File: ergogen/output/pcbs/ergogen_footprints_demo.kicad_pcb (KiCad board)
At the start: 2 copper layers, 95 x 95 mm, 51 parts

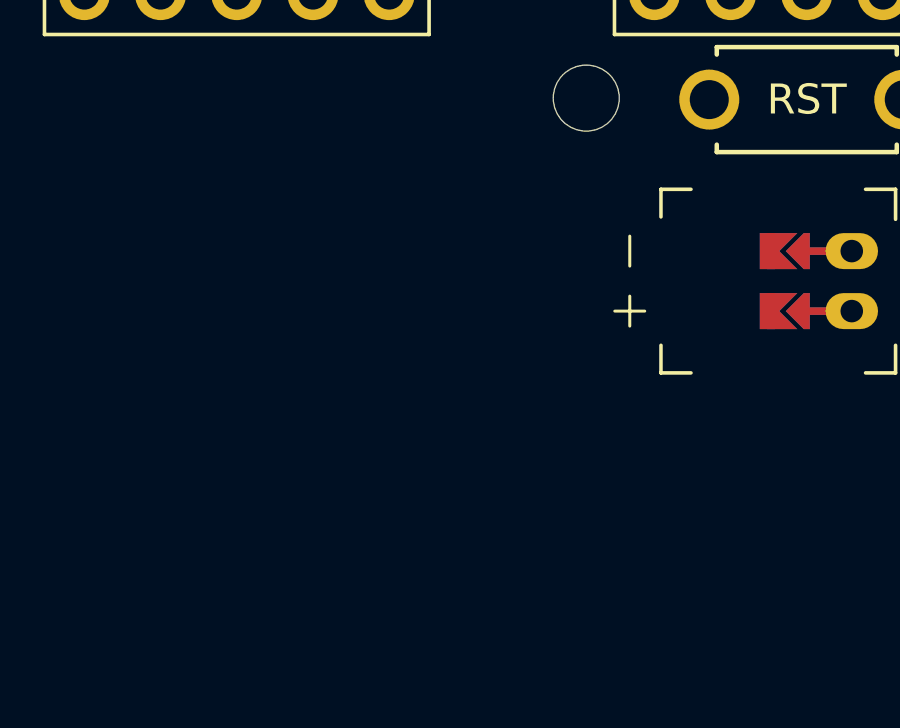
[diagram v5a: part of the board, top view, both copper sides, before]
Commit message: Add alternate power switch behavior
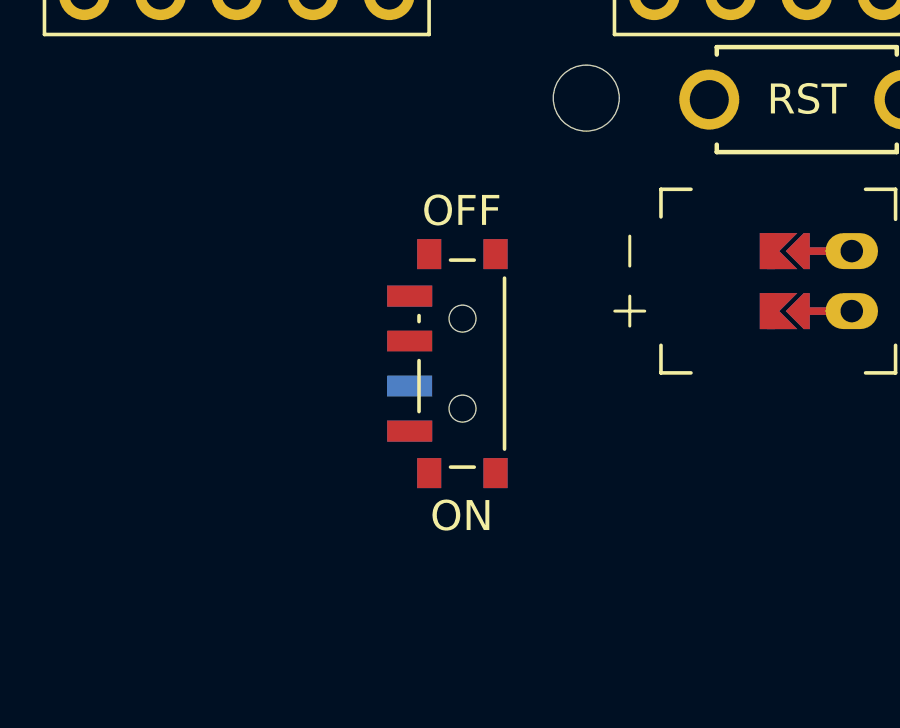
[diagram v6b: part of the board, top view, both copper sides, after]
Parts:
- added PWR2: reset_button, ceoloide:power_switch_smd_side, F.Cu at (107.5, 101.5)
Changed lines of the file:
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@@
     (segment (start 102.540 89.200) (end 102.540 87.450) (width 0.25) (layer "B.Cu") (net 63))
     (segment (start 105.080 89.200) (end 105.080 87.450) (width 0.25) (layer "B.Cu") (net 62))
+      (module "ceoloide:power_switch_smd_side" (layer F.Cu)
+        (at 107.5 101.5 0)
+        (attr smd)
+        (fp_text value "reset_button" (at 0 2.5 0) (layer F.Fab)
+          (effects (font (size 1 1) (thickness 0.15)))
+        )
+        (fp_line (start -1.305 -3.35) (end -1.305 3.35) (layer F.Fab) (width 0.1))
+        (fp_line (start 1.295 -3.35) (end -1.305 -3.35) (layer F.Fab) (width 0.1))
+        (fp_line (start 1.295 3.35) (end 1.295 -3.35) (layer F.Fab) (width 0.1))
+        (fp_line (start -1.305 3.35) (end 1.295 3.35) (layer F.Fab) (width 0.1))
+        (fp_line (start 2.595 0.1) (end 1.295 0.1) (layer F.Fab) (width 0.1))
+        (fp_line (start 2.645 0.15) (end 2.595 0.1) (layer F.Fab) (width 0.1))
+        (fp_line (start 2.845 0.35) (end 2.645 0.15) (layer F.Fab) (width 0.1))
+        (fp_line (start 2.845 1.2) (end 2.845 0.35) (layer F.Fab) (width 0.1))
+        (fp_line (start 2.645 1.4) (end 2.845 1.2) (layer F.Fab) (width 0.1))
+        (fp_line (start 1.345 1.4) (end 2.645 1.4) (layer F.Fab) (width 0.1))
+        (pad "" smd rect (at 1.125 -3.65 90) (size 1 0.8) (layers F.Cu F.Paste F.Mask))
+        (pad "" smd rect (at -1.085 -3.65 90) (size 1 0.8) (layers F.Cu F.Paste F.Mask))
+        (pad "" smd rect (at -1.085 3.65 90) (size 1 0.8) (layers F.Cu F.Paste F.Mask))
+        (pad "" smd rect (at 1.125 3.65 90) (size 1 0.8) (layers F.Cu F.Paste F.Mask))
+        (pad 1 smd rect (at -1.735 2.25 90) (size 0.7 1.5) (layers F.Cu F.Paste F.Mask) (net 97 "BAT_P"))
+        (pad 2 smd rect (at -1.735 -0.75 90) (size 0.7 1.5) (layers F.Cu F.Paste F.Mask) (net 18 "RAW"))
+        (pad 3 smd rect (at -1.735 -2.25 90) (size 0.7 1.5) (layers F.Cu F.Paste F.Mask) )
+        (fp_text reference "PWR2" (at -3.6 0 -90) (layer F.SilkS) hide
+          (effects (font (size 1 1) (thickness 0.15)))
+        )
+        (fp_text user "ON" (at 0 4.5 0) (layer "F.SilkS")
+          (effects (font (size 1 1) (thickness 0.15)) (justify top))
+        )
+        (fp_text user "OFF" (at 0 -4.5 0) (layer "F.SilkS")
+          (effects (font (size 1 1) (thickness 0.15)) (justify bottom))
+        )
+        (fp_line (start 0.415 -3.45) (end -0.375 -3.45) (layer F.SilkS) (width 0.12))
+        (fp_line (start -0.375 3.45) (end 0.415 3.45) (layer F.SilkS) (width 0.12))
+        (fp_line (start -1.425 1.6) (end -1.425 -0.1) (layer F.SilkS) (width 0.12))
+        (fp_line (start 1.425 2.85) (end 1.425 -2.85) (layer F.SilkS) (width 0.12))
+        (fp_line (start -1.425 -1.4) (end -1.425 -1.6) (layer F.SilkS) (width 0.12))
+        (fp_line (start 2.595 -0.1) (end 1.295 -0.1) (layer B.Fab) (width 0.1))
+        (fp_line (start -1.305 3.35) (end -1.305 -3.35) (layer B.Fab) (width 0.1))
+        (fp_line (start 2.645 -0.15) (end 2.595 -0.1) (layer B.Fab) (width 0.1))
+        (fp_line (start 2.845 -1.2) (end 2.845 -0.35) (layer B.Fab) (width 0.1))
+        (fp_line (start 1.345 -1.4) (end 2.645 -1.4) (layer B.Fab) (width 0.1))
+        (fp_line (start 2.845 -0.35) (end 2.645 -0.15) (layer B.Fab) (width 0.1))
+        (fp_line (start 2.645 -1.4) (end 2.845 -1.2) (layer B.Fab) (width 0.1))
+        (fp_line (start 1.295 -3.35) (end 1.295 3.35) (layer B.Fab) (width 0.1))
+        (fp_line (start 1.295 3.35) (end -1.305 3.35) (layer B.Fab) (width 0.1))
+        (fp_line (start -1.305 -3.35) (end 1.295 -3.35) (layer B.Fab) (width 0.1))
+        (pad "" smd rect (at -1.085 -3.65 270) (size 1 0.8) (layers B.Cu B.Paste B.Mask))
+        (pad "" smd rect (at 1.125 -3.65 270) (size 1 0.8) (layers B.Cu B.Paste B.Mask))
+        (pad "" smd rect (at -1.085 3.65 270) (size 1 0.8) (layers B.Cu B.Paste B.Mask))
+        (pad "" smd rect (at 1.125 3.65 270) (size 1 0.8) (layers B.Cu B.Paste B.Mask))
+        (pad 1 smd rect (at -1.735 -2.25 270) (size 0.7 1.5) (layers B.Cu B.Paste B.Mask) )
+        (pad 2 smd rect (at -1.735 0.75 270) (size 0.7 1.5) (layers B.Cu B.Paste B.Mask) (net 18 "RAW"))
+        (pad 3 smd rect (at -1.735 2.25 270) (size 0.7 1.5) (layers B.Cu B.Paste B.Mask) (net 97 "BAT_P"))
+        (fp_text user "PWR2" (at -3.5 0 90) (layer B.SilkS) hide
+          (effects (font (size 1 1) (thickness 0.15)) (justify mirror))
+        )
+        (fp_text user "ON" (at 0 4.5 0) (layer "B.SilkS")
+          (effects (font (size 1 1) (thickness 0.15)) (justify top mirror))
+        )
+        (fp_text user "OFF" (at 0 -4.5 0) (layer "B.SilkS")
+          (effects (font (size 1 1) (thickness 0.15)) (justify bottom mirror))
+        )
+        (fp_line (start -1.425 1.4) (end -1.425 1.6) (layer B.SilkS) (width 0.12))
+        (fp_line (start 0.415 3.45) (end -0.375 3.45) (layer B.SilkS) (width 0.12))
+        (fp_line (start -0.375 -3.45) (end 0.415 -3.45) (layer B.SilkS) (width 0.12))
+        (fp_line (start -1.425 -1.6) (end -1.425 0.1) (layer B.SilkS) (width 0.12))
+        (fp_line (start 1.425 -2.85) (end 1.425 2.85) (layer B.SilkS) (width 0.12))
+      (pad "" np_thru_hole circle (at 0.025 -1.5 90) (size 0.9 0.9) (drill 0.9) (layers *.Cu *.Mask))
+      (pad "" np_thru_hole circle (at 0.025 1.5 90) (size 0.9 0.9) (drill 0.9) (layers *.Cu *.Mask))
+    )
             (module "ceoloide:reset_switch_tht_top" (layer F.Cu)
                 (at 119 92.7 0)
